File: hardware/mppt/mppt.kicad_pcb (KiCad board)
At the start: 2 copper layers, 146 parts, among them IC1301 INA229AIDGSR, IC801 INA229AIDGSR, IC901 SN74LVC08APWR, IC902 SN74LVC1G04DBVR, IC903 SN74HCS367PWR, IC904 SN74LVC2G32DCUR, J301 CT3151, J302 CT3151, J303 CT3151, J304 CT3151, Q1001 Q_NMOS_SGD, Q1002 Q_NMOS_SGD, Q1101 BSS127S, Q1201 Q_NMOS_SGD, Q1202 Q_NMOS_SGD, Q501 EPC2059, Q502 EPC2059, Q601 Q_NMOS_GSD, Q701 Q_NMOS_GSD, U1001 TPSI3050, U1101 ADUM4221-1ARIZ, U1201 TPSI3050

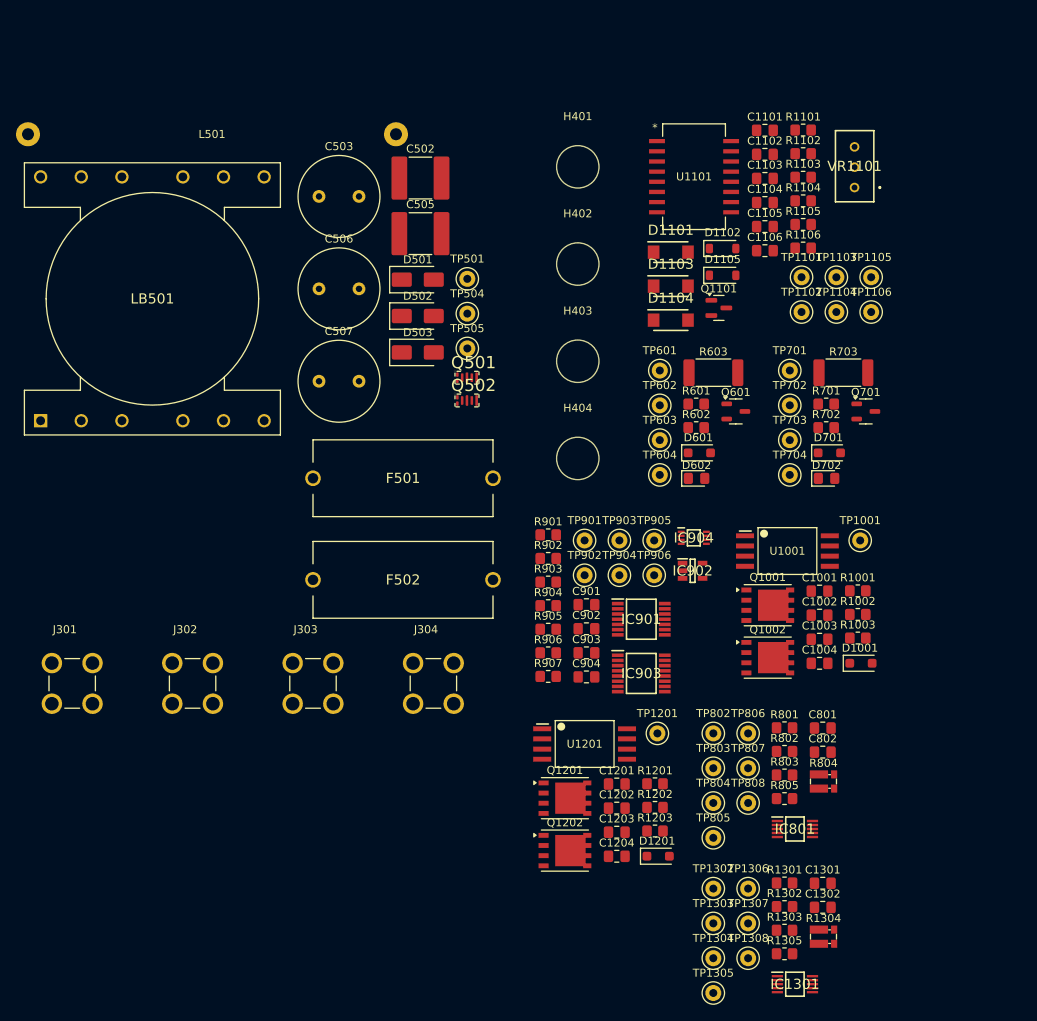
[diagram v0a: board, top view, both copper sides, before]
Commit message: update final missing pieces for sch, moving to bom pop
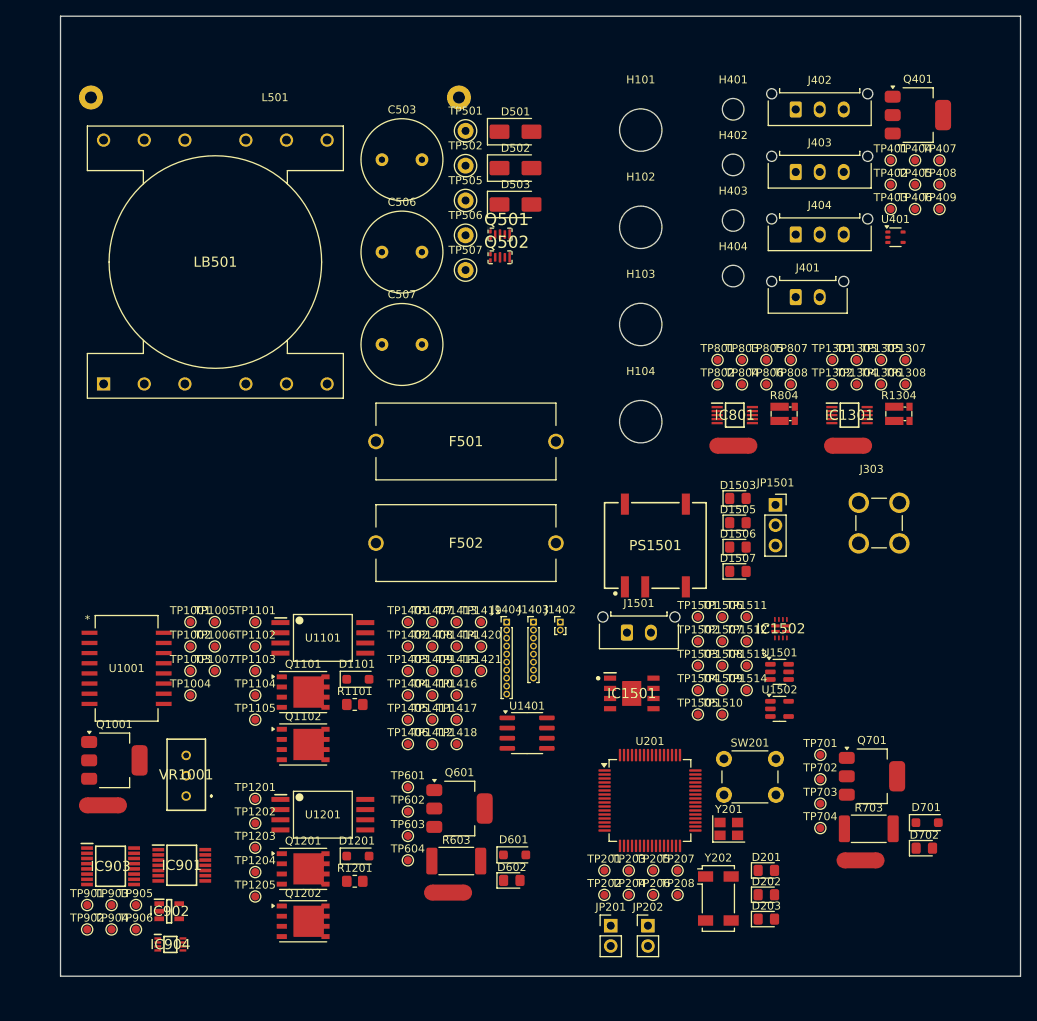
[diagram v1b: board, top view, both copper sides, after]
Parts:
- removed C1001, C1003, C1004, C1201, C1203, C1204: 1u, Capacitor_SMD:C_0805_2012Metric_Pad1.18x1.45mm_HandSolder
- removed C1002, C1102, C1105, C1106, C1202, C1301, C1302, C801, C802, C901, C902, C903, C904: 100n, Capacitor_SMD:C_0805_2012Metric_Pad1.18x1.45mm_HandSolder
- removed C1101, C1103, C1104: 10u, Capacitor_SMD:C_0805_2012Metric_Pad1.18x1.45mm_HandSolder
- removed C502, C505: 2.2u, Capacitor_SMD:C_2220_5750Metric_Pad1.97x5.40mm_HandSolder
- removed D1001: 0.35, Diode_SMD:D_SOD-123F
- removed D1102, D1105: 5.1, Diode_SMD:D_SOD-123
- removed D1103, D1104: 0.55, footprints:stm_STPS1170AF
- removed J301, J302, J304: CT3151, footprints:caltest_ct3151
- removed Q1002: Q_NMOS_SGD, Package_SO:PowerPAK_SO-8_Single
- removed R1001: 7.32k, Resistor_SMD:R_0805_2012Metric_Pad1.20x1.40mm_HandSolder
- removed R1002, R1003, R1202, R1203, R1303, R1305, R601, R602, R701, R702, R803, R805: 15, Resistor_SMD:R_0805_2012Metric_Pad1.20x1.40mm_HandSolder
- removed R1102, R1103, R1104, R1105: 0, Resistor_SMD:R_0805_2012Metric_Pad1.20x1.40mm_HandSolder
- removed R1106: 1.5, Resistor_SMD:R_0805_2012Metric_Pad1.20x1.40mm_HandSolder
- removed R1301, R801: 87.5k, Resistor_SMD:R_0805_2012Metric_Pad1.20x1.40mm_HandSolder
- removed R1302, R802: 100k, Resistor_SMD:R_0805_2012Metric_Pad1.20x1.40mm_HandSolder
- removed R901, R902, R903, R904, R905, R906, R907: 10k, Resistor_SMD:R_0805_2012Metric_Pad1.20x1.40mm_HandSolder
- removed TP1106: TestPoint_Small, TestPoint:TestPoint_Keystone_5000-5004_Miniature
- removed TP504: TestPoint, TestPoint:TestPoint_Keystone_5000-5004_Miniature
- removed VR1101: PV36W104C01B00, footprints:bourns_PV36W201C01B00
- added D1503: RED, LED_SMD:LED_0805_2012Metric_Pad1.15x1.40mm_HandSolder, F.Cu at (174.7, 90.3)
- added D1505: RED, LED_SMD:LED_0805_2012Metric_Pad1.15x1.40mm_HandSolder, F.Cu at (174.7, 93.3)
- added D1506: RED, LED_SMD:LED_0805_2012Metric_Pad1.15x1.40mm_HandSolder, F.Cu at (174.7, 96.4)
- added D1507: RED, LED_SMD:LED_0805_2012Metric_Pad1.15x1.40mm_HandSolder, F.Cu at (174.7, 99.4)
- added D201: RED, LED_SMD:LED_0805_2012Metric_Pad1.15x1.40mm_HandSolder, F.Cu at (178.2, 136.8)
- added D202: RED, LED_SMD:LED_0805_2012Metric_Pad1.15x1.40mm_HandSolder, F.Cu at (178.2, 139.8)
- added D203: RED, LED_SMD:LED_0805_2012Metric_Pad1.15x1.40mm_HandSolder, F.Cu at (178.2, 142.9)
- added H101: MountingHole, MountingHole:MountingHole_5.3mm_M5, F.Cu at (162.5, 44.2)
- added H102: MountingHole, MountingHole:MountingHole_5.3mm_M5, F.Cu at (162.5, 56.4)
- added H103: MountingHole, MountingHole:MountingHole_5.3mm_M5, F.Cu at (162.5, 68.5)
- added H104: MountingHole, MountingHole:MountingHole_5.3mm_M5, F.Cu at (162.5, 80.7)
- added IC1501: LMR38010SDDAR, footprints:ti_LMR38010_SDDAR, F.Cu at (161.4, 114.7)
- added IC1502: TPS2121, footprints:ti_TPS2121_RUXR, F.Cu at (180.0, 106.6)
- added J1402: Conn_01x02, Connector_PinHeader_1.00mm:PinHeader_1x02_P1.00mm_Vertical, F.Cu at (152.5, 105.7)
- added J1403: Conn_01x08, Connector_PinHeader_1.00mm:PinHeader_1x08_P1.00mm_Vertical, F.Cu at (149.1, 105.7)
- added J1404: Conn_01x10, Connector_PinHeader_1.00mm:PinHeader_1x10_P1.00mm_Vertical, F.Cu at (145.8, 105.7)
- added J1501: Conn_01x02, Connector_Molex:Molex_Micro-Fit_3.0_43650-0215_1x02_P3.00mm_Vertical, F.Cu at (160.8, 107.1)
- added J401: Conn_01x02, Connector_Molex:Molex_Micro-Fit_3.0_43650-0215_1x02_P3.00mm_Vertical, F.Cu at (181.9, 65.1)
- added J402: Conn_01x03, Connector_Molex:Molex_Micro-Fit_3.0_43650-0315_1x03_P3.00mm_Vertical, F.Cu at (181.9, 41.7)
- added J403: Conn_01x03, Connector_Molex:Molex_Micro-Fit_3.0_43650-0315_1x03_P3.00mm_Vertical, F.Cu at (181.9, 49.5)
- added J404: Conn_01x03, Connector_Molex:Molex_Micro-Fit_3.0_43650-0315_1x03_P3.00mm_Vertical, F.Cu at (181.9, 57.3)
- added JP1501: Jumper_3_Bridged12, Connector_PinSocket_2.54mm:PinSocket_1x03_P2.54mm_Vertical, F.Cu at (179.4, 91.1)
- added JP201: Jumper_2_Bridged, Connector_PinHeader_2.54mm:PinHeader_1x02_P2.54mm_Vertical, F.Cu at (158.8, 143.7)
- added JP202: Jumper_2_Bridged, Connector_PinHeader_2.54mm:PinHeader_1x02_P2.54mm_Vertical, F.Cu at (163.4, 143.7)
- added NT1001: NetTie_2, NetTie:NetTie-2_SMD_Pad2.0mm, F.Cu at (95.3, 128.6)
- added NT1301: NetTie_2, NetTie:NetTie-2_SMD_Pad2.0mm, F.Cu at (188.4, 83.7)
- added NT601: NetTie_2, NetTie:NetTie-2_SMD_Pad2.0mm, F.Cu at (138.4, 139.6)
- added NT701: NetTie_2, NetTie:NetTie-2_SMD_Pad2.0mm, F.Cu at (190.0, 135.5)
- added NT801: NetTie_2, NetTie:NetTie-2_SMD_Pad2.0mm, F.Cu at (174.1, 83.7)
- added PS1501: CRE1S0505MEC, footprints:murata_CRE1_S0505MEC, F.Cu at (164.4, 96.2)
- added Q1102: Q_NMOS_SGD, Package_SO:PowerPAK_SO-8_Single, F.Cu at (120.3, 121.0)
- added Q401: Q_NMOS_GDS, Package_TO_SOT_SMD:SOT-223-3_TabPin2, F.Cu at (197.2, 42.4)
- added SW201: SW_SPST, Button_Switch_THT:SW_PUSH_6mm, F.Cu at (172.9, 122.8)
- added TP1002: TestPoint_Small, TestPoint:TestPoint_Pad_D1.0mm, F.Cu at (106.2, 108.8)
- added TP1003: TestPoint_Small, TestPoint:TestPoint_Pad_D1.0mm, F.Cu at (106.2, 111.8)
- added TP1004: TestPoint_Small, TestPoint:TestPoint_Pad_D1.0mm, F.Cu at (106.2, 114.9)
- added TP1005: TestPoint_Small, TestPoint:TestPoint_Pad_D1.0mm, F.Cu at (109.3, 105.7)
- added TP1006: TestPoint_Small, TestPoint:TestPoint_Pad_D1.0mm, F.Cu at (109.3, 108.8)
- added TP1007: TestPoint_Small, TestPoint:TestPoint_Pad_D1.0mm, F.Cu at (109.3, 111.8)
- added TP1202: TestPoint_Small, TestPoint:TestPoint_Pad_D1.0mm, F.Cu at (114.3, 130.9)
- added TP1203: TestPoint_Small, TestPoint:TestPoint_Pad_D1.0mm, F.Cu at (114.3, 133.9)
- added TP1204: TestPoint_Small, TestPoint:TestPoint_Pad_D1.0mm, F.Cu at (114.3, 137.0)
- added TP1205: TestPoint_Small, TestPoint:TestPoint_Pad_D1.0mm, F.Cu at (114.3, 140.0)
- added TP1301: TestPoint_Small, TestPoint:TestPoint_Pad_D1.0mm, F.Cu at (186.5, 73.0)
- added TP1401: TestPoint_Small, TestPoint:TestPoint_Pad_D1.0mm, F.Cu at (133.4, 105.7)
- added TP1402: TestPoint_Small, TestPoint:TestPoint_Pad_D1.0mm, F.Cu at (133.4, 108.8)
- added TP1403: TestPoint_Small, TestPoint:TestPoint_Pad_D1.0mm, F.Cu at (133.4, 111.8)
- added TP1404: TestPoint_Small, TestPoint:TestPoint_Pad_D1.0mm, F.Cu at (133.4, 114.9)
- added TP1405: TestPoint_Small, TestPoint:TestPoint_Pad_D1.0mm, F.Cu at (133.4, 117.9)
- added TP1406: TestPoint_Small, TestPoint:TestPoint_Pad_D1.0mm, F.Cu at (133.4, 121.0)
- added TP1407: TestPoint_Small, TestPoint:TestPoint_Pad_D1.0mm, F.Cu at (136.5, 105.7)
- added TP1408: TestPoint_Small, TestPoint:TestPoint_Pad_D1.0mm, F.Cu at (136.5, 108.8)
- added TP1409: TestPoint_Small, TestPoint:TestPoint_Pad_D1.0mm, F.Cu at (136.5, 111.8)
- added TP1410: TestPoint_Small, TestPoint:TestPoint_Pad_D1.0mm, F.Cu at (136.5, 114.9)
- added TP1411: TestPoint_Small, TestPoint:TestPoint_Pad_D1.0mm, F.Cu at (136.5, 117.9)
- added TP1412: TestPoint_Small, TestPoint:TestPoint_Pad_D1.0mm, F.Cu at (136.5, 121.0)
- added TP1413: TestPoint_Small, TestPoint:TestPoint_Pad_D1.0mm, F.Cu at (139.5, 105.7)
- added TP1414: TestPoint_Small, TestPoint:TestPoint_Pad_D1.0mm, F.Cu at (139.5, 108.8)
- added TP1415: TestPoint_Small, TestPoint:TestPoint_Pad_D1.0mm, F.Cu at (139.5, 111.8)
- added TP1416: TestPoint_Small, TestPoint:TestPoint_Pad_D1.0mm, F.Cu at (139.5, 114.9)
- added TP1417: TestPoint_Small, TestPoint:TestPoint_Pad_D1.0mm, F.Cu at (139.5, 117.9)
- added TP1418: TestPoint_Small, TestPoint:TestPoint_Pad_D1.0mm, F.Cu at (139.5, 121.0)
- added TP1419: TestPoint_Small, TestPoint:TestPoint_Pad_D1.0mm, F.Cu at (142.6, 105.7)
- added TP1420: TestPoint_Small, TestPoint:TestPoint_Pad_D1.0mm, F.Cu at (142.6, 108.8)
- added TP1421: TestPoint_Small, TestPoint:TestPoint_Pad_D1.0mm, F.Cu at (142.6, 111.8)
- added TP1501: TestPoint_Small, TestPoint:TestPoint_Pad_D1.0mm, F.Cu at (169.7, 105.1)
- added TP1502: TestPoint_Small, TestPoint:TestPoint_Pad_D1.0mm, F.Cu at (169.7, 108.1)
- added TP1503: TestPoint_Small, TestPoint:TestPoint_Pad_D1.0mm, F.Cu at (169.7, 111.2)
- added TP1504: TestPoint_Small, TestPoint:TestPoint_Pad_D1.0mm, F.Cu at (169.7, 114.2)
- added TP1505: TestPoint_Small, TestPoint:TestPoint_Pad_D1.0mm, F.Cu at (169.7, 117.3)
- added TP1506: TestPoint_Small, TestPoint:TestPoint_Pad_D1.0mm, F.Cu at (172.7, 105.1)
- added TP1507: TestPoint_Small, TestPoint:TestPoint_Pad_D1.0mm, F.Cu at (172.7, 108.1)
- added TP1508: TestPoint_Small, TestPoint:TestPoint_Pad_D1.0mm, F.Cu at (172.7, 111.2)
- added TP1509: TestPoint_Small, TestPoint:TestPoint_Pad_D1.0mm, F.Cu at (172.7, 114.2)
- added TP1510: TestPoint_Small, TestPoint:TestPoint_Pad_D1.0mm, F.Cu at (172.7, 117.3)
- added TP1511: TestPoint_Small, TestPoint:TestPoint_Pad_D1.0mm, F.Cu at (175.8, 105.1)
- added TP1512: TestPoint_Small, TestPoint:TestPoint_Pad_D1.0mm, F.Cu at (175.8, 108.1)
- added TP1513: TestPoint_Small, TestPoint:TestPoint_Pad_D1.0mm, F.Cu at (175.8, 111.2)
- added TP1514: TestPoint_Small, TestPoint:TestPoint_Pad_D1.0mm, F.Cu at (175.8, 114.2)
- added TP201: TestPoint_Small, TestPoint:TestPoint_Pad_D1.0mm, F.Cu at (158.0, 136.8)
- added TP202: TestPoint_Small, TestPoint:TestPoint_Pad_D1.0mm, F.Cu at (158.0, 139.8)
- added TP203: TestPoint_Small, TestPoint:TestPoint_Pad_D1.0mm, F.Cu at (161.0, 136.8)
- added TP204: TestPoint_Small, TestPoint:TestPoint_Pad_D1.0mm, F.Cu at (161.0, 139.8)
- added TP205: TestPoint_Small, TestPoint:TestPoint_Pad_D1.0mm, F.Cu at (164.1, 136.8)
- added TP206: TestPoint_Small, TestPoint:TestPoint_Pad_D1.0mm, F.Cu at (164.1, 139.8)
- added TP207: TestPoint_Small, TestPoint:TestPoint_Pad_D1.0mm, F.Cu at (167.1, 136.8)
- added TP208: TestPoint_Small, TestPoint:TestPoint_Pad_D1.0mm, F.Cu at (167.1, 139.8)
- added TP401: TestPoint_Small, TestPoint:TestPoint_Pad_D1.0mm, F.Cu at (193.8, 48.0)
- added TP402: TestPoint_Small, TestPoint:TestPoint_Pad_D1.0mm, F.Cu at (193.8, 51.1)
- added TP403: TestPoint_Small, TestPoint:TestPoint_Pad_D1.0mm, F.Cu at (193.8, 54.1)
- added TP404: TestPoint_Small, TestPoint:TestPoint_Pad_D1.0mm, F.Cu at (196.8, 48.0)
- added TP405: TestPoint_Small, TestPoint:TestPoint_Pad_D1.0mm, F.Cu at (196.8, 51.1)
- added TP406: TestPoint_Small, TestPoint:TestPoint_Pad_D1.0mm, F.Cu at (196.8, 54.1)
- added TP407: TestPoint_Small, TestPoint:TestPoint_Pad_D1.0mm, F.Cu at (199.9, 48.0)
- added TP408: TestPoint_Small, TestPoint:TestPoint_Pad_D1.0mm, F.Cu at (199.9, 51.1)
- added TP409: TestPoint_Small, TestPoint:TestPoint_Pad_D1.0mm, F.Cu at (199.9, 54.1)
- added TP502: TestPoint, TestPoint:TestPoint_Keystone_5000-5004_Miniature, F.Cu at (140.6, 48.7)
- added TP506: TestPoint, TestPoint:TestPoint_Keystone_5000-5004_Miniature, F.Cu at (140.6, 57.4)
- added TP507: TestPoint, TestPoint:TestPoint_Keystone_5000-5004_Miniature, F.Cu at (140.6, 61.7)
- added TP801: TestPoint_Small, TestPoint:TestPoint_Pad_D1.0mm, F.Cu at (172.1, 73.0)
- added U1401: ISO1044BD, Package_SO:SOIC-8_3.9x4.9mm_P1.27mm, F.Cu at (148.3, 119.6)
- added U1501: AP63205WU, Package_TO_SOT_SMD:TSOT-23-6, F.Cu at (179.9, 112.0)
- added U1502: TLV75733PDBV, Package_TO_SOT_SMD:SOT-23-5, F.Cu at (179.9, 116.6)
- added U201: STM32F446RETx, Package_QFP:LQFP-64_10x10mm_P0.5mm, F.Cu at (163.7, 128.0)
- added U401: MCP9700Ax-ELT, Package_TO_SOT_SMD:SOT-353_SC-70-5, F.Cu at (194.4, 57.6)
- added VR1001: PV36W104C01B00, footprints:bourns_PV36W201C01B00, F.Cu at (105.7, 127.5)
- added Y201: 25MHz, Crystal:Crystal_SMD_Abracon_ABM8AIG-4Pin_3.2x2.5mm, F.Cu at (173.5, 131.6)
- added Y202: 32kHz, Crystal:Crystal_SMD_Abracon_ABS25-4Pin_8.0x3.8mm, F.Cu at (172.2, 140.3)
- D1101: value 0.55 -> 0.35; footprint footprints:stm_STPS1170AF -> Diode_SMD:D_SOD-123F
- H401, H402, H403, H404: footprint MountingHole:MountingHole_5.3mm_M5 -> MountingHole:MountingHole_2.7mm_M2.5
- L501: value L_Ferrite -> 471u
- Q1001: value Q_NMOS_SGD -> Q_NMOS_GDS; footprint Package_SO:PowerPAK_SO-8_Single -> Package_TO_SOT_SMD:SOT-223-3_TabPin2
- Q1101: value BSS127S -> Q_NMOS_SGD; footprint Package_TO_SOT_SMD:SOT-23 -> Package_SO:PowerPAK_SO-8_Single
- Q601, Q701: value Q_NMOS_GSD -> Q_NMOS_GDS; footprint Package_TO_SOT_SMD:SOT-23-3 -> Package_TO_SOT_SMD:SOT-223-3_TabPin2
- R1101: value 10k -> 7.32k
- TP1001, TP1101, TP1102, TP1103, TP1104, TP1105, TP1201, TP1303, TP1304, TP1305, TP1306, TP1307, TP1308, TP601, TP602, TP603, TP604, TP701, TP702, TP703, TP704, TP803, TP804, TP805, TP806, TP807, TP808, TP901, TP902, TP903, TP904, TP905, TP906: footprint TestPoint:TestPoint_Keystone_5000-5004_Miniature -> TestPoint:TestPoint_Pad_D1.0mm
- TP1302, TP802: value TestPoint -> TestPoint_Small; footprint TestPoint:TestPoint_Keystone_5000-5004_Miniature -> TestPoint:TestPoint_Pad_D1.0mm
- U1001: value TPSI3050 -> ADUM4221-1ARIZ; footprint footprints:ti_TPS3050_DWZ -> footprints:ad_ADUM4221_1ARIZ
- U1101: value ADUM4221-1ARIZ -> TPSI3050; footprint footprints:ad_ADUM4221_1ARIZ -> footprints:ti_TPS3050_DWZ
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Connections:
- net /power_converter/Power Monitor Sink/I- renamed /power_converter/OUT+
- net /power_converter/Protection Logic/MON_ALERT renamed /MON_ALERT
- C503 pad 2: GND -> /VI-
- C506 pad 2: GND -> /power_converter/OUT-
- C507 pad 2: GND -> /power_converter/OUT-
- D1101 pad 1: /power_converter/Gate Driver/VOB -> Net-(D1101-K)
- D501 pad 2: GND -> /VI-
- D502 pad 1: GND -> /VI-
- D503 pad 2: GND -> /power_converter/OUT-
- F501 pad 1: /power_converter/DCDC/VI+ -> /power_converter/Active Load Source/V+
- F502 pad 2: /power_converter/DCDC/VO+ -> /power_converter/Active Load Sink/V+
- IC1301 pad 1: /power_converter/SPI_SNK_CS -> /MON_IN_CS
- IC1301 pad 2: /power_converter/SPI_COPI -> /MON_SPI_COPI
- IC1301 pad 4: /power_converter/SPI_CIPO -> /MON_SPI_CIPO
- IC1301 pad 5: /power_converter/SPI_CLK -> /MON_SPI_CLK
- IC801 pad 1: /power_converter/SPI_SRC_CS -> /MON_OUT_CS
- IC801 pad 2: /power_converter/SPI_COPI -> /MON_SPI_COPI
- IC801 pad 4: /power_converter/SPI_CIPO -> /MON_SPI_CIPO
- IC801 pad 5: /power_converter/SPI_CLK -> /MON_SPI_CLK
- IC901 pad 10: /power_converter/CONV_EN -> /CONV_EN
- IC901 pad 2: /power_converter/LS_SRC_EN -> /LS_IN_EN
- IC901 pad 5: /power_converter/LS_SNK_EN -> /LS_OUT_EN
- IC903 pad 1: /power_converter/PROT_DIS -> /PROT_DISABLE
- IC903 pad 11: /power_converter/CONV_EN_BUF -> /power_converter/Gate Driver/CONV_EN
- IC903 pad 13: /power_converter/CONV_PWM_BUF -> /power_converter/Gate Driver/CONV_PWM
- IC903 pad 14: /power_converter/CONV_PWM -> /CONV_PWM
- IC903 pad 15: /power_converter/CONV_DIS -> /CONV_DISABLE
- IC904 pad 2: /power_converter/AL_SRC_EN -> /AL_IN_EN
- IC904 pad 6: /power_converter/AL_SNK_EN -> /AL_OUT_EN
- J303 pad 1: /power_converter/VO+ -> /VI+
- J303 pad 2: /power_converter/VO+ -> /VI+
- J303 pad 3: /power_converter/VO+ -> /VI+
- J303 pad 4: /power_converter/VO+ -> /VI+
- Q1001 pad 1: /power_converter/Load Switch Source/VSSS -> /power_converter/Gate Driver/CONV_EN
- Q1001 pad 2: Net-(D1001-A) -> /power_converter/Gate Driver/DISABLE
- Q1001 pad 3: /power_converter/Load Switch Source/I+ -> GND
- Q1101 pad 1: /power_converter/CONV_EN_BUF -> /power_converter/Load Switch Source/VSSS
- Q1101 pad 2: GND -> Net-(D1101-A)
- Q1101 pad 3: /power_converter/Gate Driver/DISABLE -> /power_converter/Active Load Sink/V+
- Q1202 pad 3: /power_converter/Load Switch Sink/I- -> /power_converter/Active Load Source/V+
- Q501 pad 2: GND -> /VI-
- Q501 pad 4: GND -> /VI-
- Q501 pad 6: GND -> /VI-
- Q601 pad 2: /power_converter/Active Load Sink/V- -> Net-(Q601-D)
- Q601 pad 3: Net-(Q601-D) -> /power_converter/OUT-
- Q701 pad 2: /power_converter/Active Load Source/V- -> Net-(Q701-D)
- Q701 pad 3: Net-(Q701-D) -> /VI-
- R1101 pad 1: +3V3 -> Net-(U1101-PXFR)
- R1101 pad 2: /power_converter/Gate Driver/DISABLE -> GND
- R1304 pad 1: /power_converter/Power Monitor Sink/I+ -> /power_converter/Load Switch Source/I-
- R804 pad 1: /power_converter/Power Monitor Source/I+ -> /VI+
- R804 pad 4: /power_converter/Power Monitor Source/I- -> /power_converter/Load Switch Sink/I+
- TP1001 pad 1: Net-(U1001-VDDH) -> +3V3
- TP1101 pad 1: /power_converter/SWL -> +3V3
- TP1102 pad 1: /power_converter/VSW -> GND
- TP1103 pad 1: GND -> /power_converter/Load Switch Source/VDRV
- TP1104 pad 1: Net-(U1101-VDDA) -> /power_converter/Load Switch Source/VDDH
- TP1105 pad 1: +5V -> /power_converter/Load Switch Source/VSSS
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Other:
- board outline added: 120 x 120 mm

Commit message: bom consolidated, starting layout
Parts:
- removed JP202: Jumper_2_Bridged, Connector_PinHeader_2.54mm:PinHeader_1x02_P2.54mm_Vertical
- added C1001: 10u, Capacitor_SMD:C_1206_3216Metric_Pad1.33x1.80mm_HandSolder, F.Cu at (129.2, 191.6)
- added C1002: 100n, Capacitor_SMD:C_0402_1005Metric_Pad0.74x0.62mm_HandSolder, F.Cu at (150.4, 193.1)
- added C1003: 10u, Capacitor_SMD:C_1206_3216Metric_Pad1.33x1.80mm_HandSolder, F.Cu at (129.2, 195.0)
- added C1004: 10u, Capacitor_SMD:C_1206_3216Metric_Pad1.33x1.80mm_HandSolder, F.Cu at (129.2, 198.3)
- added C1005: 100n, Capacitor_SMD:C_0402_1005Metric_Pad0.74x0.62mm_HandSolder, F.Cu at (150.4, 195.0)
- added C1006: 100n, Capacitor_SMD:C_0402_1005Metric_Pad0.74x0.62mm_HandSolder, F.Cu at (150.4, 197.0)
- added C1101: 1u, Capacitor_SMD:C_0603_1608Metric_Pad1.08x0.95mm_HandSolder, F.Cu at (164.0, 217.2)
- added C1102: 100n, Capacitor_SMD:C_0402_1005Metric_Pad0.74x0.62mm_HandSolder, F.Cu at (163.4, 227.0)
- added C1103: 1u, Capacitor_SMD:C_0603_1608Metric_Pad1.08x0.95mm_HandSolder, F.Cu at (164.0, 219.7)
- added C1104: 1u, Capacitor_SMD:C_0603_1608Metric_Pad1.08x0.95mm_HandSolder, F.Cu at (164.0, 222.2)
- added C1201: 1u, Capacitor_SMD:C_0603_1608Metric_Pad1.08x0.95mm_HandSolder, F.Cu at (59.7, 207.2)
- added C1202: 100n, Capacitor_SMD:C_0402_1005Metric_Pad0.74x0.62mm_HandSolder, F.Cu at (59.1, 216.9)
- added C1203: 1u, Capacitor_SMD:C_0603_1608Metric_Pad1.08x0.95mm_HandSolder, F.Cu at (59.7, 209.7)
- added C1204: 1u, Capacitor_SMD:C_0603_1608Metric_Pad1.08x0.95mm_HandSolder, F.Cu at (59.7, 212.2)
- added C1301: 100n, Capacitor_SMD:C_0402_1005Metric_Pad0.74x0.62mm_HandSolder, F.Cu at (190.1, 219.3)
- added C1302: 100n, Capacitor_SMD:C_0402_1005Metric_Pad0.74x0.62mm_HandSolder, F.Cu at (190.1, 221.2)
- added C1401: 100n, Capacitor_SMD:C_0402_1005Metric_Pad0.74x0.62mm_HandSolder, B.Cu at (111.0, 75.5)
- added C1402: 100n, Capacitor_SMD:C_0402_1005Metric_Pad0.74x0.62mm_HandSolder, B.Cu at (116.0, 75.5)
- added C1501: 1u, Capacitor_SMD:C_0603_1608Metric_Pad1.08x0.95mm_HandSolder, F.Cu at (68.6, 149.8)
- added C1502: 2.2u, Capacitor_SMD:C_2220_5750Metric_Pad1.97x5.40mm_HandSolder, F.Cu at (118.1, 152.0)
- added C1503: 2.2u, Capacitor_SMD:C_2220_5750Metric_Pad1.97x5.40mm_HandSolder, F.Cu at (118.1, 159.0)
- added C1504: 1u, Capacitor_SMD:C_0603_1608Metric_Pad1.08x0.95mm_HandSolder, F.Cu at (68.6, 152.3)
- added C1505: 100n, Capacitor_SMD:C_1206_3216Metric_Pad1.33x1.80mm_HandSolder, F.Cu at (119.3, 120.3)
- added C1506: 100n, Capacitor_SMD:C_0402_1005Metric_Pad0.74x0.62mm_HandSolder, F.Cu at (124.1, 149.6)
- added C1507: 1u, Capacitor_SMD:C_0603_1608Metric_Pad1.08x0.95mm_HandSolder, F.Cu at (68.6, 154.8)
- added C1508: 22u, Capacitor_SMD:C_1210_3225Metric_Pad1.33x2.70mm_HandSolder, F.Cu at (110.7, 150.7)
- added C1509: 22u, Capacitor_SMD:C_1210_3225Metric_Pad1.33x2.70mm_HandSolder, F.Cu at (110.7, 154.9)
- added C1510: 10u, Capacitor_SMD:C_1206_3216Metric_Pad1.33x1.80mm_HandSolder, F.Cu at (119.3, 123.6)
- added C1511: 22u, Capacitor_SMD:C_1210_3225Metric_Pad1.33x2.70mm_HandSolder, F.Cu at (110.7, 159.2)
- added C1512: 1u, Capacitor_SMD:C_0603_1608Metric_Pad1.08x0.95mm_HandSolder, F.Cu at (68.6, 157.3)
- added C1513: 10u, Capacitor_SMD:C_1206_3216Metric_Pad1.33x1.80mm_HandSolder, F.Cu at (119.3, 127.0)
- added C1514: 100n, Capacitor_SMD:C_0402_1005Metric_Pad0.74x0.62mm_HandSolder, F.Cu at (124.1, 151.5)
- added C1515: 4.7u, Capacitor_SMD:C_0805_2012Metric_Pad1.18x1.45mm_HandSolder, F.Cu at (104.3, 168.2)
- added C1516: 22u, Capacitor_SMD:C_1210_3225Metric_Pad1.33x2.70mm_HandSolder, F.Cu at (110.7, 163.4)
- added C1517: 22u, Capacitor_SMD:C_1210_3225Metric_Pad1.33x2.70mm_HandSolder, F.Cu at (110.7, 167.7)
- added C201: 10p, Capacitor_SMD:C_0402_1005Metric_Pad0.74x0.62mm_HandSolder, B.Cu at (77.0, 72.5)
- added C202: 15p, Capacitor_SMD:C_0402_1005Metric_Pad0.74x0.62mm_HandSolder, B.Cu at (80.5, 66.0)
- added C203: 100n, Capacitor_SMD:C_0402_1005Metric_Pad0.74x0.62mm_HandSolder, B.Cu at (66.0, 75.0)
- added C204: 10u, Capacitor_SMD:C_1206_3216Metric_Pad1.33x1.80mm_HandSolder, B.Cu at (90.6, 72.5)
- added C205: 100n, Capacitor_SMD:C_0402_1005Metric_Pad0.74x0.62mm_HandSolder, B.Cu at (93.0, 69.5)
- added C206: 10p, Capacitor_SMD:C_0402_1005Metric_Pad0.74x0.62mm_HandSolder, B.Cu at (77.0, 74.5)
- added C207: 15p, Capacitor_SMD:C_0402_1005Metric_Pad0.74x0.62mm_HandSolder, B.Cu at (80.6, 69.0)
- added C208: 100n, Capacitor_SMD:C_0402_1005Metric_Pad0.74x0.62mm_HandSolder, B.Cu at (85.5, 69.0)
- added C209: 100n, Capacitor_SMD:C_0402_1005Metric_Pad0.74x0.62mm_HandSolder, B.Cu at (93.0, 76.5)
- added C210: 4.7u, Capacitor_SMD:C_0805_2012Metric_Pad1.18x1.45mm_HandSolder, B.Cu at (91.0, 76.0)
- added C211: 100n, Capacitor_SMD:C_0402_1005Metric_Pad0.74x0.62mm_HandSolder, B.Cu at (86.0, 77.0)
- added C212: 100n, Capacitor_SMD:C_0402_1005Metric_Pad0.74x0.62mm_HandSolder, B.Cu at (85.5, 70.5)
- added C213: 100n, Capacitor_SMD:C_0402_1005Metric_Pad0.74x0.62mm_HandSolder, B.Cu at (85.0, 75.0)
- added C214: 1u, Capacitor_SMD:C_0603_1608Metric_Pad1.08x0.95mm_HandSolder, B.Cu at (86.0, 73.0)
- added C401: 1u, Capacitor_SMD:C_0603_1608Metric_Pad1.08x0.95mm_HandSolder, F.Cu at (37.5, 82.6)
- added C402: 1u, Capacitor_SMD:C_0603_1608Metric_Pad1.08x0.95mm_HandSolder, F.Cu at (37.5, 85.1)
- added C501: 100n, Capacitor_SMD:C_1206_3216Metric_Pad1.33x1.80mm_HandSolder, F.Cu at (79.6, 272.6)
- added C502: 1u, Capacitor_SMD:C_2220_5750Metric_Pad1.97x5.40mm_HandSolder, F.Cu at (117.6, 234.3)
- added C504: 18u, Capacitor_THT:C_Radial_D10.0mm_H16.0mm_P5.00mm, F.Cu at (104.9, 236.6)
- added C505: 100n, Capacitor_SMD:C_1206_3216Metric_Pad1.33x1.80mm_HandSolder, F.Cu at (79.6, 276.0)
- added C508: 18u, Capacitor_THT:C_Radial_D10.0mm_H16.0mm_P5.00mm, F.Cu at (104.9, 248.2)
- added C509: 18u, Capacitor_THT:C_Radial_D10.0mm_H16.0mm_P5.00mm, F.Cu at (104.9, 259.7)
- added C801: 100n, Capacitor_SMD:C_0402_1005Metric_Pad0.74x0.62mm_HandSolder, F.Cu at (39.0, 225.3)
- added C802: 100n, Capacitor_SMD:C_0402_1005Metric_Pad0.74x0.62mm_HandSolder, F.Cu at (39.0, 227.3)
- added C901: 100n, Capacitor_SMD:C_0402_1005Metric_Pad0.74x0.62mm_HandSolder, F.Cu at (108.4, 197.1)
- added C902: 100n, Capacitor_SMD:C_0402_1005Metric_Pad0.74x0.62mm_HandSolder, F.Cu at (108.4, 199.1)
- added C903: 100n, Capacitor_SMD:C_0402_1005Metric_Pad0.74x0.62mm_HandSolder, F.Cu at (108.4, 201.0)
- added C904: 100n, Capacitor_SMD:C_0402_1005Metric_Pad0.74x0.62mm_HandSolder, F.Cu at (108.4, 203.0)
- added D1001: Schottky, Diode_SMD:D_SOD-123F, F.Cu at (141.7, 177.0)
- added D1002: Zener, Diode_SMD:D_SOD-123F, F.Cu at (141.7, 180.3)
- added D1003: Schottky, Diode_SMD:D_SOD-123F, F.Cu at (141.7, 183.7)
- added D1004: Schottky, Diode_SMD:D_SOD-123F, F.Cu at (141.7, 187.1)
- added D1005: Zener, Diode_SMD:D_SOD-123F, F.Cu at (141.7, 190.4)
- added D1501: SMAJ15CA, Diode_SMD:D_SMA_Handsoldering, F.Cu at (96.9, 165.6)
- added D1502: SMAJ15CA, Diode_SMD:D_SMA_Handsoldering, F.Cu at (96.9, 170.2)
- added D1504: Schottky, Diode_SMD:D_SOD-123F, F.Cu at (104.7, 165.0)
- added D401: Schottky, Diode_SMD:D_SOD-123F, F.Cu at (38.1, 103.9)
- added FB201: FerriteBead, Resistor_SMD:R_0603_1608Metric_Pad0.98x0.95mm_HandSolder, B.Cu at (87.4, 75.5)
- added J1401: Conn_01x04, Connector_Molex:Molex_Micro-Fit_3.0_43650-0415_1x04_P3.00mm_Vertical, F.Cu at (135.5, 77.4)
- added J1405: USB_C_Plug_USB2.0, Connector_USB:USB_C_Receptacle_GCT_USB4105-xx-A_16P_TopMnt_Horizontal, F.Cu at (126.9, 66.0)
- added J1502: CT3151, footprints:caltest_ct3151, F.Cu at (73.9, 123.2)
- added J1503: CT3151, footprints:caltest_ct3151, F.Cu at (89.0, 123.2)
- added J1504: CT3151, footprints:caltest_ct3151, F.Cu at (104.0, 123.2)
- added J301: Conn_01x01, footprints:ke_7771_SEMS, F.Cu at (241.9, 86.4)
- added J302: Conn_01x01, footprints:ke_7771_SEMS, F.Cu at (253.0, 86.4)
- added J304: CT3151, footprints:caltest_ct3151, F.Cu at (226.3, 51.0)
- added J305: CT3151, footprints:caltest_ct3151, F.Cu at (241.4, 51.0)
- added J306: CT3151, footprints:caltest_ct3151, F.Cu at (256.4, 51.0)
- added J307: Conn_01x01, footprints:ke_7771_SEMS, F.Cu at (264.1, 86.4)
- added J308: Conn_01x01, footprints:ke_7771_SEMS, F.Cu at (275.2, 86.4)
- added L1501: 68u, Inductor_SMD:L_Bourns_SRN6045TA, F.Cu at (87.8, 152.3)
- added L1502: 4.7u, Inductor_SMD:L_Bourns_SRN6045TA, F.Cu at (87.8, 159.9)
- added L1503: 10u, Inductor_SMD:L_Bourns_SRN6045TA, F.Cu at (87.8, 167.4)
- added NT1501: NetTie_2, NetTie:NetTie-2_SMD_Pad2.0mm, F.Cu at (115.0, 144.9)
- added NT501: NetTie_3_Tee, NetTie:NetTie-3_SMD_Pad2.0mm, F.Cu at (82.1, 269.5)
- added R1001: 10k, Resistor_SMD:R_0603_1608Metric_Pad0.98x0.95mm_HandSolder, F.Cu at (135.2, 197.6)
- added R1002: 0, Resistor_SMD:R_1210_3225Metric_Pad1.30x2.65mm_HandSolder, F.Cu at (136.0, 177.4)
- added R1003: 0, Resistor_SMD:R_1210_3225Metric_Pad1.30x2.65mm_HandSolder, F.Cu at (136.0, 181.6)
- added R1004: 0, Resistor_SMD:R_1210_3225Metric_Pad1.30x2.65mm_HandSolder, F.Cu at (136.0, 185.8)
- added R1005: 0, Resistor_SMD:R_1210_3225Metric_Pad1.30x2.65mm_HandSolder, F.Cu at (136.0, 190.1)
- added R1006: 1.5, Resistor_SMD:R_1210_3225Metric_Pad1.30x2.65mm_HandSolder, F.Cu at (136.0, 194.3)
- added R1102: 15, Resistor_SMD:R_1210_3225Metric_Pad1.30x2.65mm_HandSolder, F.Cu at (169.2, 218.1)
- added R1103: 15, Resistor_SMD:R_1210_3225Metric_Pad1.30x2.65mm_HandSolder, F.Cu at (169.2, 222.3)
- added R1202: 15, Resistor_SMD:R_1210_3225Metric_Pad1.30x2.65mm_HandSolder, F.Cu at (64.8, 208.0)
- added R1203: 15, Resistor_SMD:R_1210_3225Metric_Pad1.30x2.65mm_HandSolder, F.Cu at (64.8, 212.2)
- added R1301: 86.6k, Resistor_SMD:R_0603_1608Metric_Pad0.98x0.95mm_HandSolder, F.Cu at (178.9, 219.5)
- added R1302: 100k, Resistor_SMD:R_0603_1608Metric_Pad0.98x0.95mm_HandSolder, F.Cu at (178.9, 222.0)
- added R1303: 15, Resistor_SMD:R_0603_1608Metric_Pad0.98x0.95mm_HandSolder, F.Cu at (178.9, 224.5)
- added R1305: 15, Resistor_SMD:R_0603_1608Metric_Pad0.98x0.95mm_HandSolder, F.Cu at (178.9, 227.1)
- added R1401: 120, Resistor_SMD:R_0603_1608Metric_Pad0.98x0.95mm_HandSolder, B.Cu at (118.0, 76.5)
- added R1402: 100k, Resistor_SMD:R_0603_1608Metric_Pad0.98x0.95mm_HandSolder, B.Cu at (101.9, 51.5)
- added R1403: 100k, Resistor_SMD:R_0603_1608Metric_Pad0.98x0.95mm_HandSolder, B.Cu at (101.9, 54.0)
- added R1404: 100k, Resistor_SMD:R_0603_1608Metric_Pad0.98x0.95mm_HandSolder, B.Cu at (101.9, 56.5)
- added R1405: 5.1k, Resistor_SMD:R_0603_1608Metric_Pad0.98x0.95mm_HandSolder, B.Cu at (119.6, 63.0)
- added R1406: 5.1k, Resistor_SMD:R_0603_1608Metric_Pad0.98x0.95mm_HandSolder, B.Cu at (119.5, 69.0)
- added R1501: 100k, Resistor_SMD:R_0603_1608Metric_Pad0.98x0.95mm_HandSolder, F.Cu at (68.6, 159.9)
- added R1502: 10k, Resistor_SMD:R_0603_1608Metric_Pad0.98x0.95mm_HandSolder, F.Cu at (68.6, 162.4)
- added R1503: 100k, Resistor_SMD:R_0603_1608Metric_Pad0.98x0.95mm_HandSolder, F.Cu at (72.9, 149.8)
- added R1504: 7.68k, Resistor_SMD:R_0603_1608Metric_Pad0.98x0.95mm_HandSolder, F.Cu at (72.9, 152.3)
- added R1505: 100k, Resistor_SMD:R_0603_1608Metric_Pad0.98x0.95mm_HandSolder, F.Cu at (72.9, 154.8)
- added R1506: 7.68k, Resistor_SMD:R_0603_1608Metric_Pad0.98x0.95mm_HandSolder, F.Cu at (72.9, 157.3)
- added R1507: 64.9k, Resistor_SMD:R_0603_1608Metric_Pad0.98x0.95mm_HandSolder, F.Cu at (72.9, 159.9)
- added R1508: 100k, Resistor_SMD:R_0603_1608Metric_Pad0.98x0.95mm_HandSolder, F.Cu at (72.9, 162.4)
- added R1509: 17.4k, Resistor_SMD:R_0603_1608Metric_Pad0.98x0.95mm_HandSolder, F.Cu at (77.3, 149.8)
- added R1510: 100k, Resistor_SMD:R_0603_1608Metric_Pad0.98x0.95mm_HandSolder, F.Cu at (77.3, 152.3)
- added R1511: 14k, Resistor_SMD:R_0603_1608Metric_Pad0.98x0.95mm_HandSolder, F.Cu at (77.3, 154.8)
- added R1512: 64.9k, Resistor_SMD:R_0603_1608Metric_Pad0.98x0.95mm_HandSolder, F.Cu at (77.3, 157.3)
- added R1513: 100k, Resistor_SMD:R_0603_1608Metric_Pad0.98x0.95mm_HandSolder, F.Cu at (77.3, 159.9)
- added R1514: 100k, Resistor_SMD:R_0603_1608Metric_Pad0.98x0.95mm_HandSolder, F.Cu at (77.3, 162.4)
- added R1515: 10k, Resistor_SMD:R_0603_1608Metric_Pad0.98x0.95mm_HandSolder, F.Cu at (81.6, 149.8)
- added R1516: 10k, Resistor_SMD:R_0603_1608Metric_Pad0.98x0.95mm_HandSolder, F.Cu at (81.6, 152.3)
- added R1517: 10k, Resistor_SMD:R_0603_1608Metric_Pad0.98x0.95mm_HandSolder, F.Cu at (81.6, 154.8)
- added R1518: 3.3k, Resistor_SMD:R_0603_1608Metric_Pad0.98x0.95mm_HandSolder, F.Cu at (81.6, 157.3)
- added R1519: 3.3k, Resistor_SMD:R_0603_1608Metric_Pad0.98x0.95mm_HandSolder, F.Cu at (81.6, 159.9)
- added R1520: 3.3k, Resistor_SMD:R_0603_1608Metric_Pad0.98x0.95mm_HandSolder, F.Cu at (81.6, 162.4)
- added R201: 3.3k, Resistor_SMD:R_0603_1608Metric_Pad0.98x0.95mm_HandSolder, B.Cu at (97.5, 74.6)
- added R202: 3.3k, Resistor_SMD:R_0603_1608Metric_Pad0.98x0.95mm_HandSolder, B.Cu at (100.0, 74.6)
- added R203: 0, Resistor_SMD:R_1210_3225Metric_Pad1.30x2.65mm_HandSolder, B.Cu at (80.5, 73.0)
- added R204: 10k, Resistor_SMD:R_0603_1608Metric_Pad0.98x0.95mm_HandSolder, F.Cu at (87.0, 64.1)
- added R205: 3.3k, Resistor_SMD:R_0603_1608Metric_Pad0.98x0.95mm_HandSolder, B.Cu at (102.5, 74.6)
- added R401: 3.3k, Resistor_SMD:R_0603_1608Metric_Pad0.98x0.95mm_HandSolder, F.Cu at (37.5, 87.6)
- added R402: 3.3k, Resistor_SMD:R_0603_1608Metric_Pad0.98x0.95mm_HandSolder, F.Cu at (37.5, 90.2)
- added R403: 205, Resistor_SMD:R_0603_1608Metric_Pad0.98x0.95mm_HandSolder, F.Cu at (37.5, 92.7)
- added R601: 15, Resistor_SMD:R_1210_3225Metric_Pad1.30x2.65mm_HandSolder, F.Cu at (142.4, 220.8)
- added R602: 15, Resistor_SMD:R_1210_3225Metric_Pad1.30x2.65mm_HandSolder, F.Cu at (142.4, 225.0)
- added R701: 15, Resistor_SMD:R_1210_3225Metric_Pad1.30x2.65mm_HandSolder, F.Cu at (85.7, 209.9)
- added R702: 15, Resistor_SMD:R_1210_3225Metric_Pad1.30x2.65mm_HandSolder, F.Cu at (85.7, 214.1)
- added R801: 86.6k, Resistor_SMD:R_0603_1608Metric_Pad0.98x0.95mm_HandSolder, F.Cu at (27.8, 225.6)
- added R802: 100k, Resistor_SMD:R_0603_1608Metric_Pad0.98x0.95mm_HandSolder, F.Cu at (27.8, 228.1)
- added R803: 15, Resistor_SMD:R_0603_1608Metric_Pad0.98x0.95mm_HandSolder, F.Cu at (27.8, 230.6)
- added R805: 15, Resistor_SMD:R_0603_1608Metric_Pad0.98x0.95mm_HandSolder, F.Cu at (27.8, 233.1)
- added R901: 10k, Resistor_SMD:R_0603_1608Metric_Pad0.98x0.95mm_HandSolder, F.Cu at (95.8, 184.6)
- added R902: 10k, Resistor_SMD:R_0603_1608Metric_Pad0.98x0.95mm_HandSolder, F.Cu at (95.8, 187.1)
- added R903: 10k, Resistor_SMD:R_0603_1608Metric_Pad0.98x0.95mm_HandSolder, F.Cu at (95.8, 189.6)
- added R904: 10k, Resistor_SMD:R_0603_1608Metric_Pad0.98x0.95mm_HandSolder, F.Cu at (95.8, 192.1)
- added R905: 10k, Resistor_SMD:R_0603_1608Metric_Pad0.98x0.95mm_HandSolder, F.Cu at (95.8, 194.7)
- added R906: 10k, Resistor_SMD:R_0603_1608Metric_Pad0.98x0.95mm_HandSolder, F.Cu at (95.8, 197.2)
- added R907: 10k, Resistor_SMD:R_0603_1608Metric_Pad0.98x0.95mm_HandSolder, F.Cu at (95.8, 199.7)
- added TP1309: TestPoint_2Pole, TestPoint:TestPoint_2Pads_Pitch2.54mm_Drill0.8mm, F.Cu at (182.9, 224.6)
- added TP1310: TestPoint_2Pole, TestPoint:TestPoint_2Pads_Pitch2.54mm_Drill0.8mm, F.Cu at (182.9, 227.9)
- added TP209: TestPoint_Small, TestPoint:TestPoint_Pad_D1.0mm, F.Cu at (91.0, 56.0)
- added TP210: TestPoint_Small, TestPoint:TestPoint_Pad_D1.0mm, F.Cu at (88.5, 56.0)
- added TP301: TestPoint, TestPoint:TestPoint_Keystone_5000-5004_Miniature, F.Cu at (286.1, 48.6)
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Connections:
- IC1501 pad 1: /VI- -> GND
- J1403 pad 2: GND -> /SWDIO
- J1403 pad 3: /SWDIO -> /USART_TX
- J1403 pad 5: /NRST -> /USART_RX
- J1403 pad 6: /USART_TX -> /NRST
- J1403 pad 7: /USART_RX -> GND
- JP201 pad 1: Net-(JP201-A) -> GND
- JP201 pad 2: +3V3 -> Net-(JP201-C)
- TP1402 pad 1: GND -> +5VL
- TP1403 pad 1: +5VL -> GND
- TP201 pad 1: /controller/RESERVED0 -> +3V3
- TP202 pad 1: /controller/RESERVED1 -> GND
- TP203 pad 1: /controller/RESERVED2 -> /controller/RESERVED0
- TP204 pad 1: /controller/RESERVED3 -> /controller/RESERVED1
- TP205 pad 1: /controller/RESERVED4 -> /controller/RESERVED2
- TP206 pad 1: /controller/RESERVED5 -> /controller/RESERVED3
- TP207 pad 1: /controller/RESERVED6 -> /controller/RESERVED4
- TP208 pad 1: /controller/RESERVED7 -> /controller/RESERVED5
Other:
- board size 120 x 120 mm -> 160 x 160 mm

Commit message: progress on layout
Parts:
- removed TP1310: TestPoint_2Pole, TestPoint:TestPoint_2Pads_Pitch2.54mm_Drill0.8mm
- removed TP801: TestPoint_Small, TestPoint:TestPoint_Pad_D1.0mm
- C1204, C1502, C1504, C1505, C1506, C1509, C1510, C1511, C1514, C1515, C1517, C401, C402, D1201, D1501, D401, IC1301, IC1501, IC1502, IC801, L1501, L1502, L1503, NT1301, NT801, R1201, R1302, R1303, R1305, R1501, R1502, R1504, R1506, R1507, R1509, R1511, R1512, R1513, R1514, R1515, R1516, R1517, R1518, R1519, R1520, R401, R402, R403, R802, R803, R805, U1201, U1501, U1502: moved to B.Cu
- TP1308: value TestPoint_Small -> TestPoint_2Pole; footprint TestPoint:TestPoint_Pad_D1.0mm -> TestPoint:TestPoint_2Pads_Pitch2.54mm_Drill0.8mm
- moved C1512 292.0 mm to (360.3, 170.8), turned to 90 degrees
- moved R1519 288.6 mm to (370.2, 152.9), turned to -90 degrees
- moved R1518 288.3 mm to (369.6, 170.5), turned to 90 degrees
- moved C1507 284.5 mm to (353.1, 152.7)
- moved TP1501 276.4 mm to (342.6, 129.6)
- moved TP1502 276.4 mm to (342.6, 133.9)
- moved TP1505 276.4 mm to (351.3, 129.6)
- moved TP1506 276.4 mm to (351.3, 133.9)
- moved TP1503 276.4 mm to (346.9, 129.6)
- moved TP1504 276.4 mm to (346.9, 133.9)
- moved TP1507 276.4 mm to (355.6, 129.6)
- moved TP1508 276.4 mm to (355.6, 133.9)
- moved R1512 275.9 mm to (353.1, 152.7)
- moved C1504 274.6 mm to (343.1, 156.4), turned to 180 degrees
- moved C1501 274.5 mm to (343.1, 148.9), turned to 180 degrees
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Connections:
- R1301 pad 1: /power_converter/OUT+ -> /power_converter/Load Switch Source/I-
- R801 pad 1: /VI+ -> /power_converter/Load Switch Sink/I+
- TP1301 pad 1: GND -> /MON_SPI_CLK
- TP1302 pad 1: /MON_SPI_CLK -> /MON_SPI_CIPO
- TP1303 pad 1: /MON_SPI_CIPO -> /MON_SPI_COPI
- TP1304 pad 1: /MON_SPI_COPI -> /MON_IN_CS
- TP1305 pad 1: /MON_IN_CS -> /power_converter/~{MON_ALERT}
- TP1306 pad 1: /power_converter/~{MON_ALERT} -> +3V3
- TP1307 pad 1: +3V3 -> GND
- TP1308 pad 1: GND -> /power_converter/Power Monitor Sink/VBUS
- TP1309 pad 1: /power_converter/Power Monitor Sink/VBUS -> /power_converter/Power Monitor Sink/IN+
- TP1309 pad 2: GND -> /power_converter/Power Monitor Sink/IN-
- TP809 pad 2: GND -> /VI-
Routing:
- net Net-(IC1501-EN): track 0.00 -> 8.54 mm
- net /power regulation/BUCK_PG: track 0.00 -> 3.56 mm
- net /power regulation/BUCK_FB: track 0.00 -> 1.85 mm
- net /VI+: track 0.00 -> 1.84 mm
- net Net-(IC1501-RT/SYNC): track 0.00 -> 1.73 mm
- net Net-(R1514-Pad2): track 0.00 -> 1.47 mm
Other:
- copper layers 2 -> 4

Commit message: placement of majority of power path
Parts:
- added REF**: Symbol_HighVoltage_Triangle_6x6mm_Copper, Symbol:Symbol_HighVoltage_Triangle_6x6mm_Copper, F.Cu at (138.0, 195.1)
- added REF**: OSHW-Logo2_9.8x8mm_Copper, Symbol:OSHW-Logo2_9.8x8mm_Copper, F.Cu at (49.3, 196.1)
- added REF**: KiCad-Logo_5mm_Copper, Symbol:KiCad-Logo_5mm_Copper, F.Cu at (32.3, 188.1)
- added REF**: Symbol_HighVoltage_Triangle_6x6mm_Copper, Symbol:Symbol_HighVoltage_Triangle_6x6mm_Copper, F.Cu at (19.1, 195.1)
- C1001, C1002, C1003, C1004, C1005, C1006, C1104, C501, C503, C505, C507, D1001, D1002, D1003, D1004, D1005, D1101, R1006, R1101, R601, R602, R603, R701, R702, R703, U1101: moved to B.Cu
- moved R1303 171.4 mm to (161.6, 113.6)
- moved TP1302 171.4 mm to (164.9, 103.7)
- moved TP1304 171.4 mm to (161.3, 105.8)
- moved TP1306 171.4 mm to (164.9, 107.7)
- moved C1301 171.4 mm to (162.9, 112.7)
- moved C1302 171.4 mm to (166.7, 108.3)
- moved IC1301 171.4 mm to (163.7, 105.8)
- moved NT1301 171.4 mm to (156.4, 110.2)
- moved R1301 171.4 mm to (158.9, 113.6)
- moved R1302 171.4 mm to (158.9, 113.6)
- moved R1305 171.4 mm to (164.2, 113.6)
- moved TP1301 171.4 mm to (166.1, 105.8)
- moved TP1303 171.4 mm to (162.5, 103.7)
- moved TP1305 171.4 mm to (163.7, 105.8)
- moved TP1307 171.4 mm to (162.5, 107.7)
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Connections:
- C505 pad 2: /power_converter/OUT- -> /VI-
- D1002 pad 2: GND -> GNDPWR
- R1003 pad 2: GND -> GNDPWR
- TP503 pad 1: GND -> GNDPWR
- TP505 pad 1: GND -> GNDPWR
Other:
- board text added: "-"
- board text added: "0-80V"
- board text added: "80-150V"
- board text added: "BANANA FOR SCALE"
- board text added: "Mighty MPPT Power Converter Breakout v0.1.0rc Matthew Yu & Jacob Pustilnik"
- board text added: "SERNO."
